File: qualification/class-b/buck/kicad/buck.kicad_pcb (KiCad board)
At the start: 4 copper layers, 63 x 37.6 mm, 20 parts, among them J1 24V_IN, J2 3V3_OUT, U1 TPS54202DDCR

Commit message: SYN-67 - Re-export the buck board on current main and give it its own case
Re-ran the whole chain on main 1eac8a1 (KiCad 10.0.7, FreeRouting 2.4.1,
OpenJDK 25.0.5). The exporter's 1.5 mm edge rim (#272) shrinks the outline
from 63.0 x 37.6 mm to 58.0 x 32.6 mm; every part position is unchanged,
and three export runs gave byte-identical KiCad files.

Adds the manufacturing exports #38 asks for: 22 Gerbers plus the job file,
PTH and NPTH drill files, and pick-and-place. Adds a second release report,
because asking for the fab package flips the same board from release_ready
true to untrusted on the 7 unreviewed parts; both answers are kept.

QUALIFICATION.md is rewritten around this board instead of a shared
template: the A rows are the measurements above, the B rows name the
capability-descriptor limits they rest on (thermal_relief_analysis,
power_sequencing_and_power_good, split_ground_planes,
return_path_and_layer_transition_analysis), and a new section maps every
#38 "Check exactly" line to a verdict for this board. It also carries the
[[board]] row this board declares for qualification/matrix.toml, with no
expect value invented: synth check cannot select FreeRouting at this
revision and no KiCadRoutingTools checkout was available to measure it.

Also corrects stale claims: the negative twin has 13 warnings not 14, the
schematic's net names now match the PCB, and the MCP placement review
passes (score 100) instead of reporting a stale outline.

Signed-off-by: nyagamunene <stevenyaga2014@gmail.com>
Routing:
- net GND: vias 4 -> 14
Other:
- board size 63 x 37.6 mm -> 58 x 32.6 mm

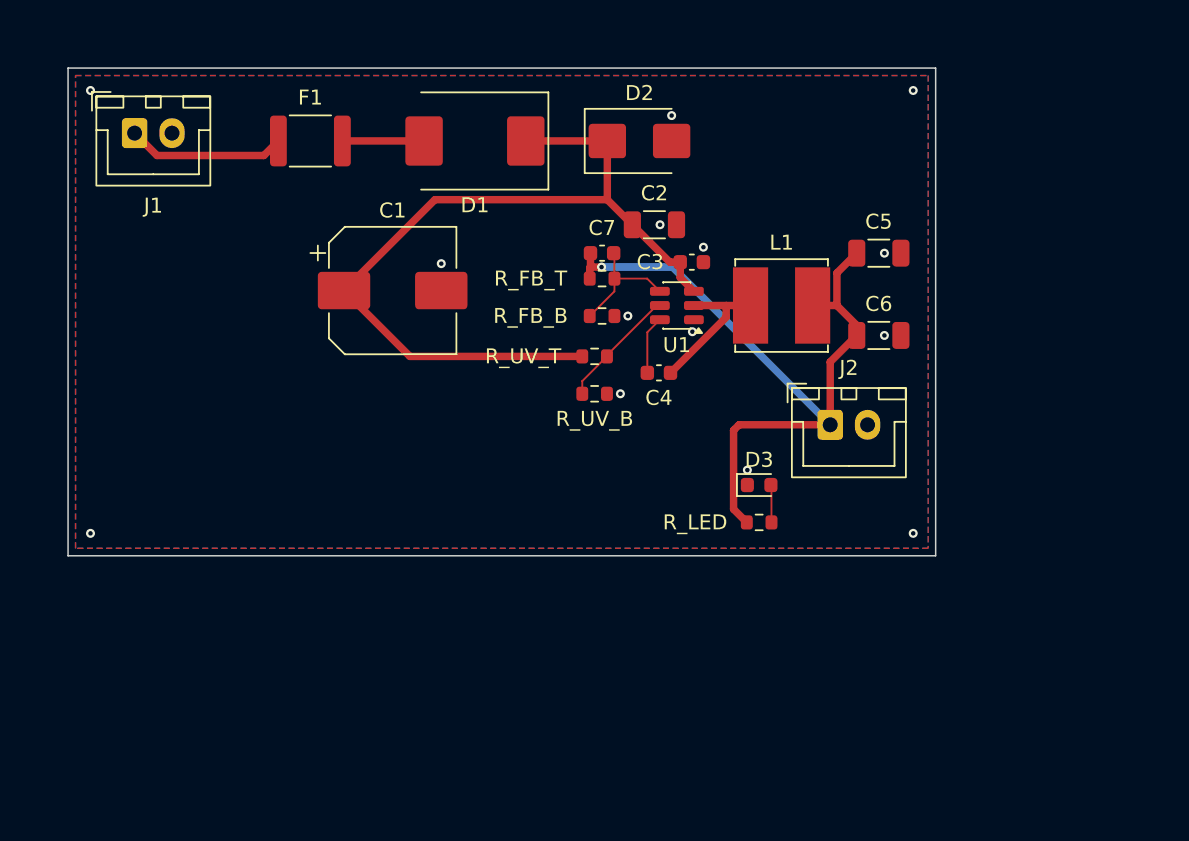
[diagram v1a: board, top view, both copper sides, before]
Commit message: SYN-67 - Rebuild the buck board around it and re-prove the A rows
25 components including two M2.5 mounting holes, a 4-pin output connector
(+3V3, GND, PG, GND) and the values from LMR33640 Table 9-2: 6.8 uH, 3x
22 uF out, 10 uF + 220 nF in, 1 uF VCC, 100 nF boot, 100k/43.2k feedback,
56 pF feed-forward, 1.37M/100k UVLO (18.1 V / 16.6 V). PG is open drain and
pulled up through 100k.

Re-routed with FreeRouting 2.4.1 on main 1eac8a1: 12 nets, 0 open, 81
segments, 18 vias, 0 blocking findings. Outline 71.9 x 31.1 mm. KiCad DRC
0/0/30 (5 are silkscreen, new with the denser placement), ERC 0/68. Two
exports byte-identical; gerbers, drill, BOM, pick-and-place and images
regenerated; 50 hashes rewritten.

QUALIFICATION.md now proves the power-good net and the thermal pad (A15,
A16) and keeps their behaviour unverified (B3, B2). The overvoltage row is
bounded honestly: a sustained 28-32 V rail is inside the 36 V rating, a
surge is not covered because the TVS clamps above the 38 V absolute max.

Signed-off-by: nyagamunene <stevenyaga2014@gmail.com>
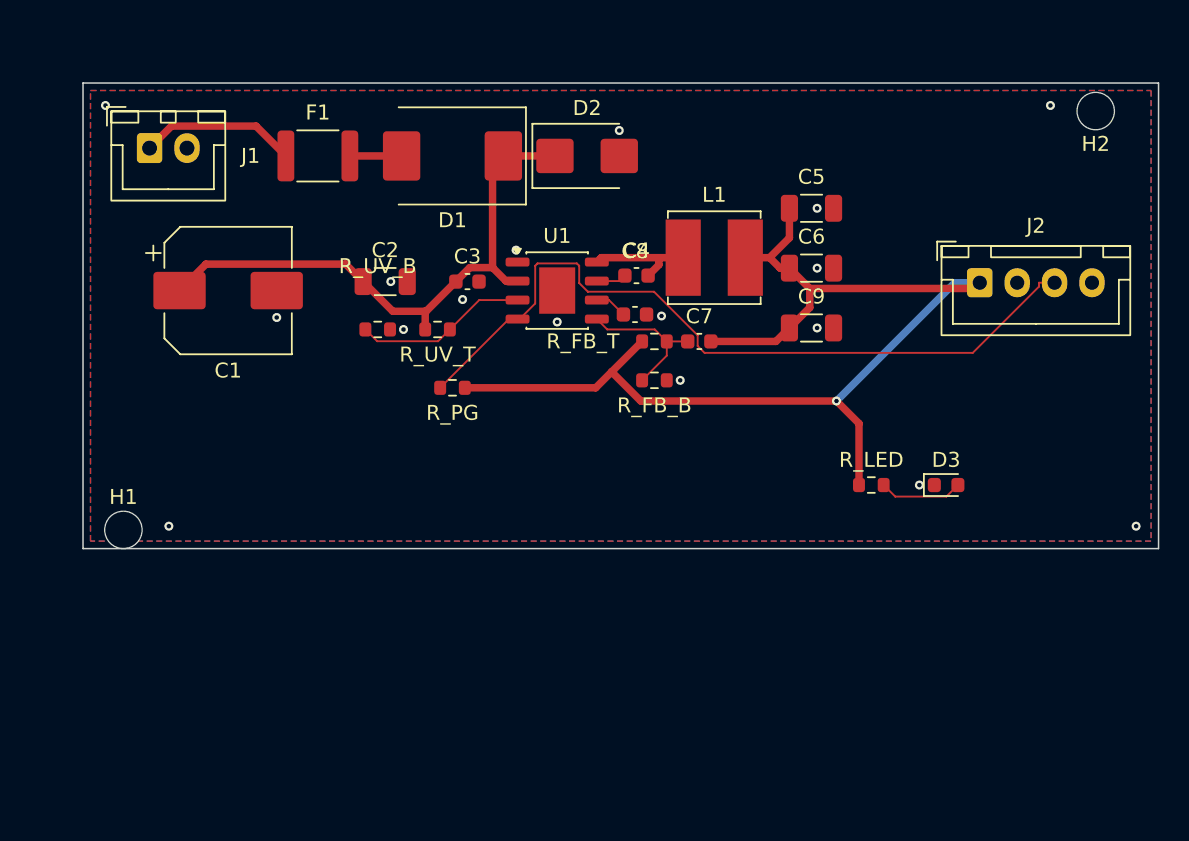
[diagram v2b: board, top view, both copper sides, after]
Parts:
- added C8: 1uF, Capacitor_SMD:C_0603_1608Metric, F.Cu at (38.2, 17.6)
- added C9: 22uF, Capacitor_SMD:C_1206_3216Metric, F.Cu at (50.0, 18.5)
- added H1: M2.5, MountingHole:MountingHole_2.5mm, F.Cu at (4.00, 32.0)
- added H2: M2.5, MountingHole:MountingHole_2.5mm, F.Cu at (69.0, 4.00)
- added R_PG: 100k, Resistor_SMD:R_0603_1608Metric, F.Cu at (26.0, 22.5)
- C3: value 100nF -> 220nF
- D2: value SMBJ26A -> SMBJ30A
- J2: footprint Connector_JST:JST_XH_B2B-XH-A_1x02_P2.50mm_Vertical -> Connector_JST:JST_XH_B4B-XH-A_1x04_P2.50mm_Vertical
- L1: value 10uH -> 6.8uH
- R_FB_B: value 22.1k -> 43.2k
- R_UV_T: value 1.5M -> 1.37M
- U1: value TPS54202DDCR -> LMR33640ADDA; footprint Package_TO_SOT_SMD:SOT-23-6 -> Package_SO:HSOP-8-1EP_3.9x4.9mm_P1.27mm_EP2.41x3.1mm
- moved C2 18.4 mm to (21.5, 15.4)
- moved R_UV_B 15.1 mm to (21.0, 18.6)
- moved C3 15.1 mm to (27.0, 15.4)
- moved J2 13.8 mm to (61.2, 15.5)
- moved D3 12.5 mm to (59.0, 29.0)
- moved C1 11.0 mm to (11.0, 16.0)
- moved R_UV_T 10.7 mm to (25.0, 18.6)
- moved C7 8.78 mm to (42.5, 19.4), turned to 0 degrees
- moved U1 8.06 mm to (33.0, 16.0), turned to 0 degrees
- moved R_LED 7.91 mm to (54.0, 29.0)
- moved C4 6.67 mm to (38.3, 15.0)
- moved C6 6.36 mm to (50.0, 14.5)
- moved R_FB_B 5.54 mm to (39.5, 22.0)
- moved L1 5.52 mm to (43.5, 13.8)
- moved R_FB_T 5.47 mm to (39.5, 19.4)
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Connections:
- U1 pad 2: SW -> VIN
- U1 pad 3: VIN -> EN
- U1 pad 4: FB -> PG
- U1 pad 5: EN -> FB
- U1 pad 6: BOOT -> U1_VCC
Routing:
- net PG: track 0.00 -> 51.7 mm
- net +3V3: track 50.2 -> 77.4 mm
- net VIN: track 56.2 -> 38.6 mm
- net EN: track 8.17 -> 11.6 mm
- net LED_PWR: track 2.52 -> 5.60 mm
- net SW: track 9.83 -> 7.40 mm
- net U1_VCC: track 0.00 -> 2.17 mm
- net VIN_FUSED: track 5.46 -> 3.46 mm
- net BOOT: track 3.90 -> 2.03 mm
- net FB: track 8.29 -> 9.98 mm
- net GND: vias 14 -> 17
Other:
- board size 58 x 32.6 mm -> 71.9 x 31.1 mm

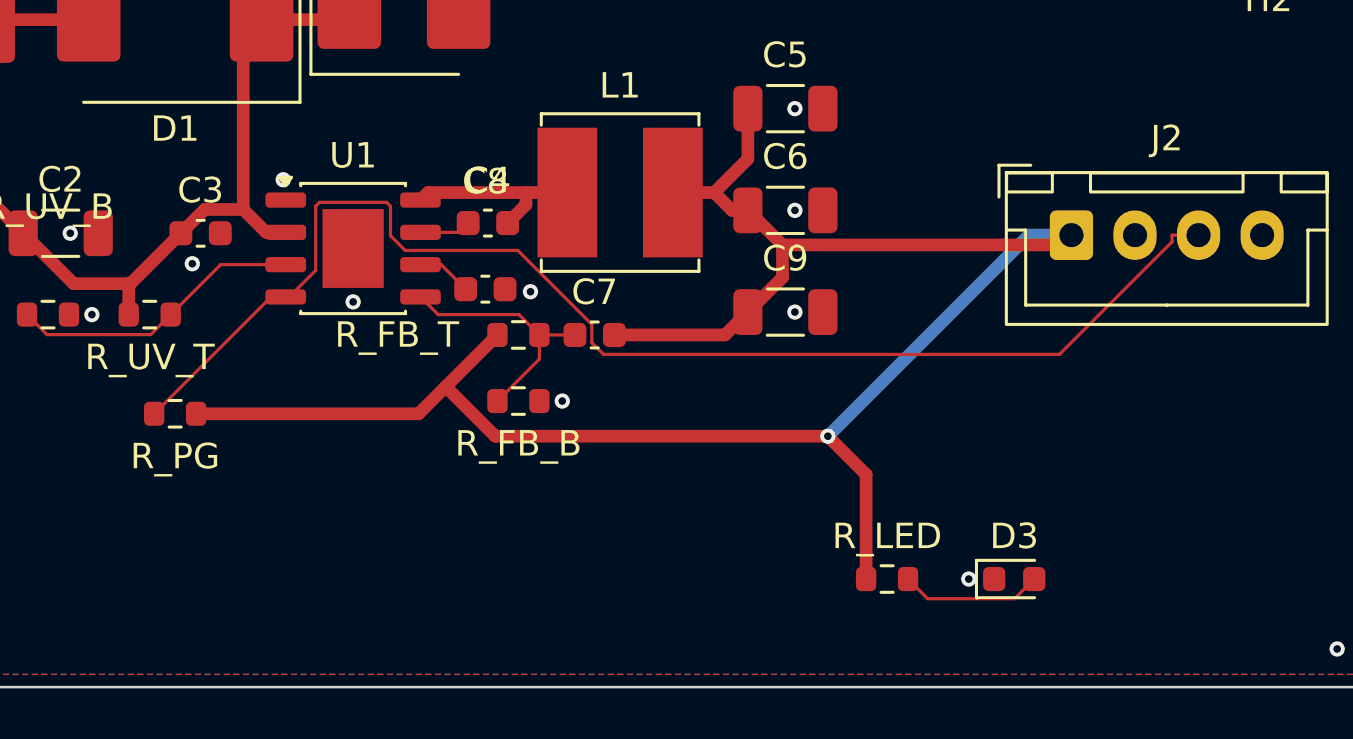
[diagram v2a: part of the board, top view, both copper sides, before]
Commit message: SYN-67 - Add a power-good fault LED to the buck board
D4 and R_PGLED run from +3V3 to PG, so the LED lights while the open-drain PG pin is low. Reuses the existing ltst_c190kgkt part, no registry change. Adding the two parts re-ran the router, so the KiCad files, reports, renders and hashes are regenerated and the docs carry the new numbers (13 nets, 27 parts, 16 GND vias).

Signed-off-by: nyagamunene <stevenyaga2014@gmail.com>
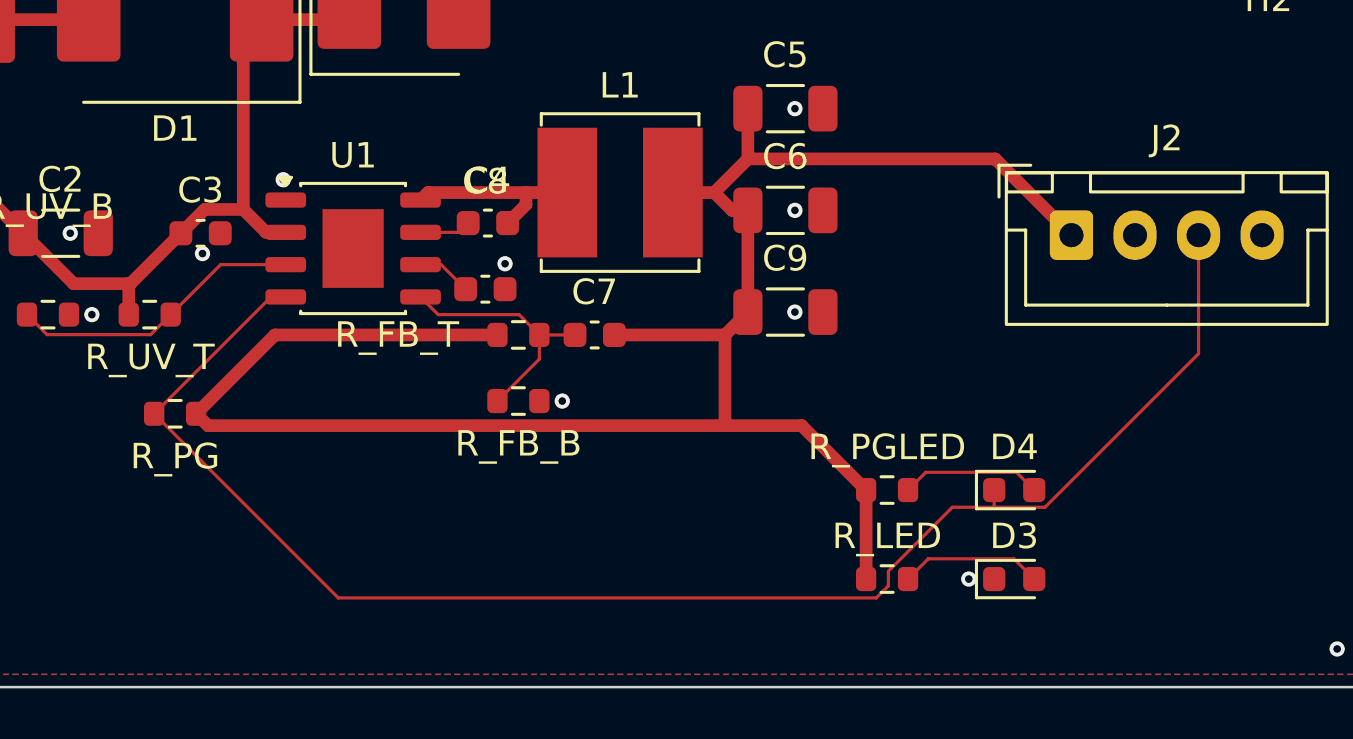
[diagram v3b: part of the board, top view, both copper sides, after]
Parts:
- added D4: PG FAULT, LED_SMD:LED_0603_1608Metric, F.Cu at (59.0, 25.5)
- added R_PGLED: 470, Resistor_SMD:R_0603_1608Metric, F.Cu at (54.0, 25.5)
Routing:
- net PG: track 51.7 -> 60.8 mm
- net LED_PG: track 0.00 -> 5.54 mm
- net +3V3: track 77.4 -> 78.5 mm, vias 1 -> 0
- net GND: vias 17 -> 16

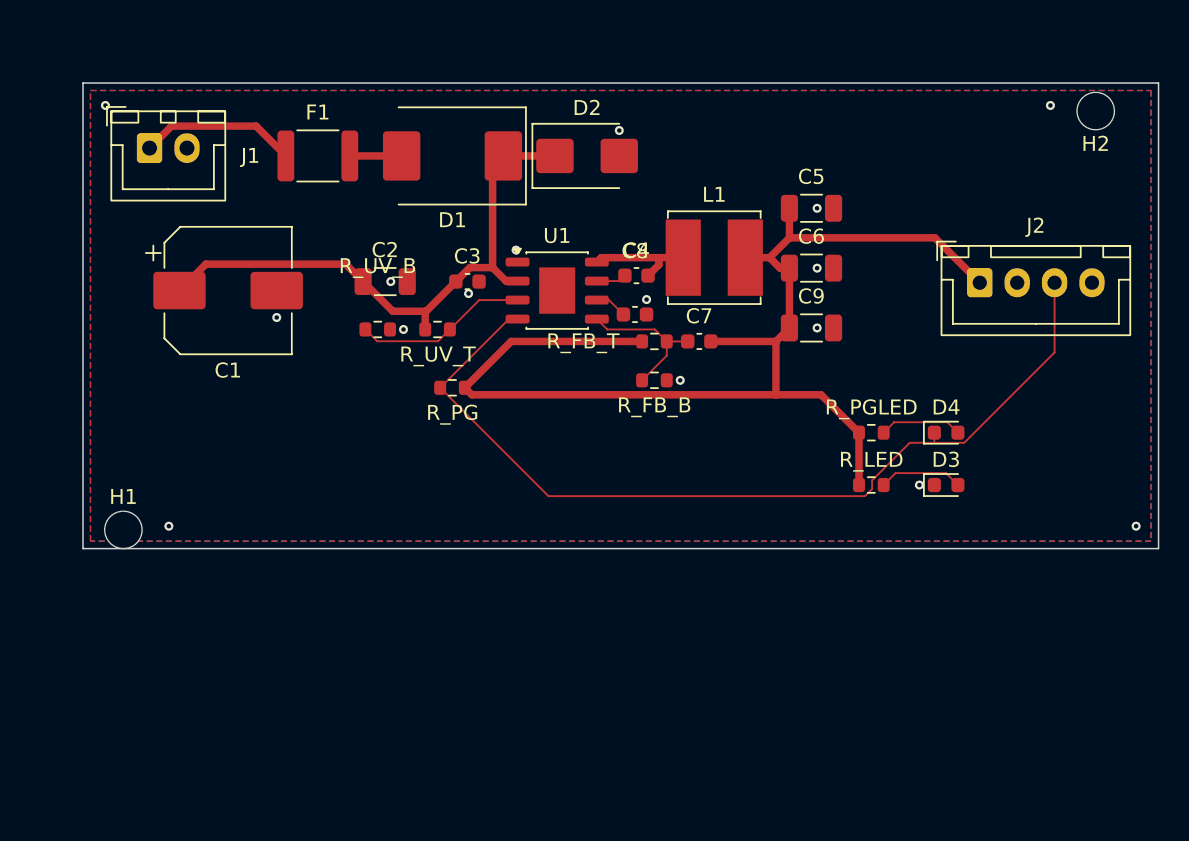
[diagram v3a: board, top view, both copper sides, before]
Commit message: SYN-67 - Re-place the buck board with Synth's own placer on current main
The sidecar now pins only the two mounting holes; the rest is placed with --place-route-iterate on main 2054046. Routes with 0 open nets and 0 DRC errors, but the board is 67.6 x 48.09 mm and the decoupling loops are long (C3 27 mm from VIN), so B5 and B12 now say it likely fails. KiCad files, reports, renders, hashes and docs are regenerated.

Signed-off-by: nyagamunene <stevenyaga2014@gmail.com>
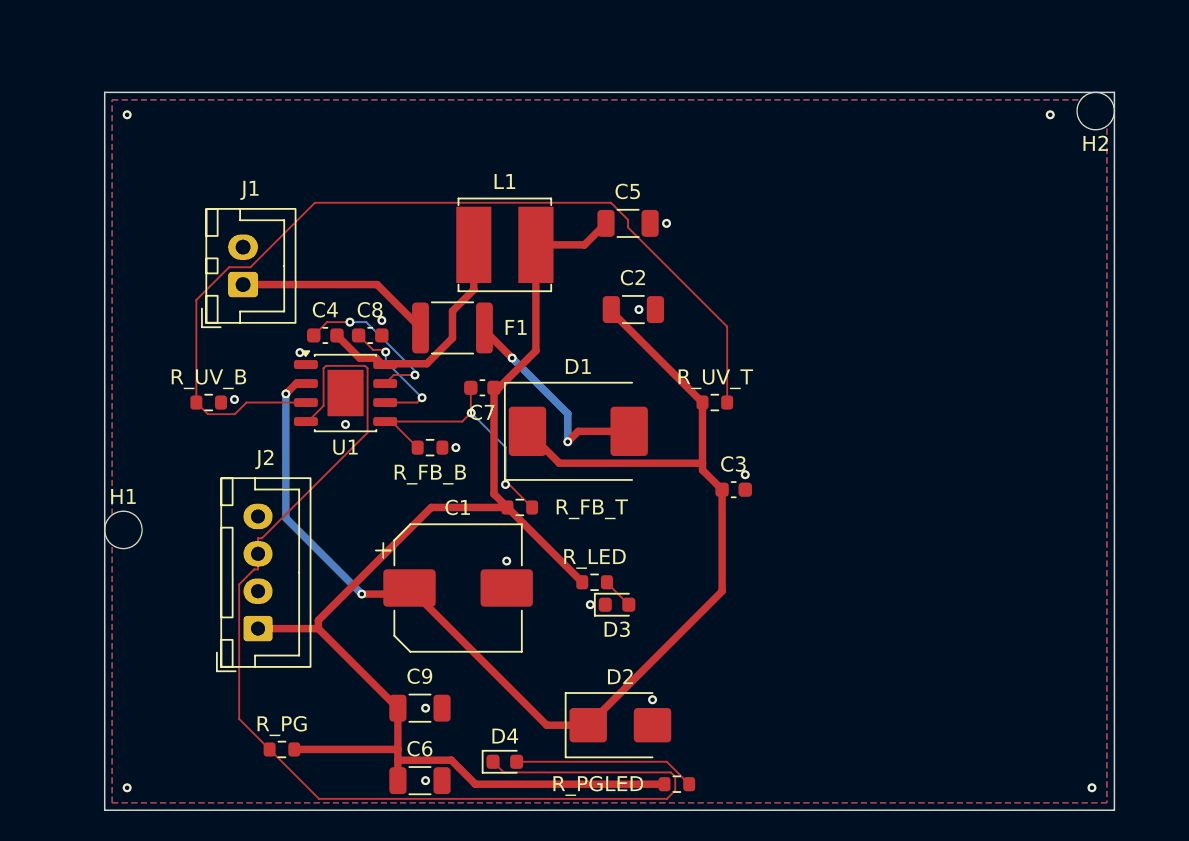
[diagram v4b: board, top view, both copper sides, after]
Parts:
- moved J2 53.5 mm to (13.0, 38.6), turned to 90 degrees
- moved C6 43.1 mm to (23.8, 48.8)
- moved D2 38.1 mm to (37.2, 45.1)
- moved D4 36.8 mm to (29.5, 47.5)
- moved C9 36.5 mm to (23.8, 43.9)
- moved R_PGLED 26.9 mm to (41.0, 49.0)
- moved R_PG 26.7 mm to (14.6, 46.7)
- moved C1 25.1 mm to (26.4, 35.9)
- moved D3 23.4 mm to (37.0, 37.0)
- moved C3 22.6 mm to (44.8, 29.3)
- moved C4 21.2 mm to (17.5, 19.0)
- moved D1 20.2 mm to (34.4, 25.4), turned to 0 degrees
- moved R_LED 19.6 mm to (35.5, 35.5)
- moved R_UV_T 19.2 mm to (43.5, 23.5)
- moved C8 17.8 mm to (20.5, 19.0)
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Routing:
- net EN: track 11.6 -> 61.8 mm
- net VIN: track 38.6 -> 83.4 mm, vias 0 -> 2
- net PG: track 60.8 -> 79.6 mm
- net +3V3: track 78.5 -> 89.8 mm
- net VIN_FUSED: track 3.46 -> 14.3 mm, vias 0 -> 2
- net BOOT: track 2.03 -> 11.0 mm, vias 0 -> 2
- net SW: track 7.40 -> 16.1 mm
- net FB: track 9.98 -> 18.5 mm, vias 0 -> 2
- net U1_VCC: track 2.17 -> 8.93 mm, vias 0 -> 2
- net LED_PG: track 5.54 -> 12.2 mm
- net LED_PWR: track 5.62 -> 2.11 mm
- net VIN_RAW: track 10.5 -> 13.1 mm
- net GND: vias 16 -> 17
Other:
- board size 71.9 x 31.1 mm -> 67.5 x 48 mm
